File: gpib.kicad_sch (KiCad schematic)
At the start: 5 parts, among them U1 SN74LVC8T245PWR, U2 SN74LVC07APWR, U6 SN74LVC1G07DCKR, U7 SN74LVC14APWR

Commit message: Start work on PCB
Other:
- moved on the sheet: R8, U1, U2, U6, U7

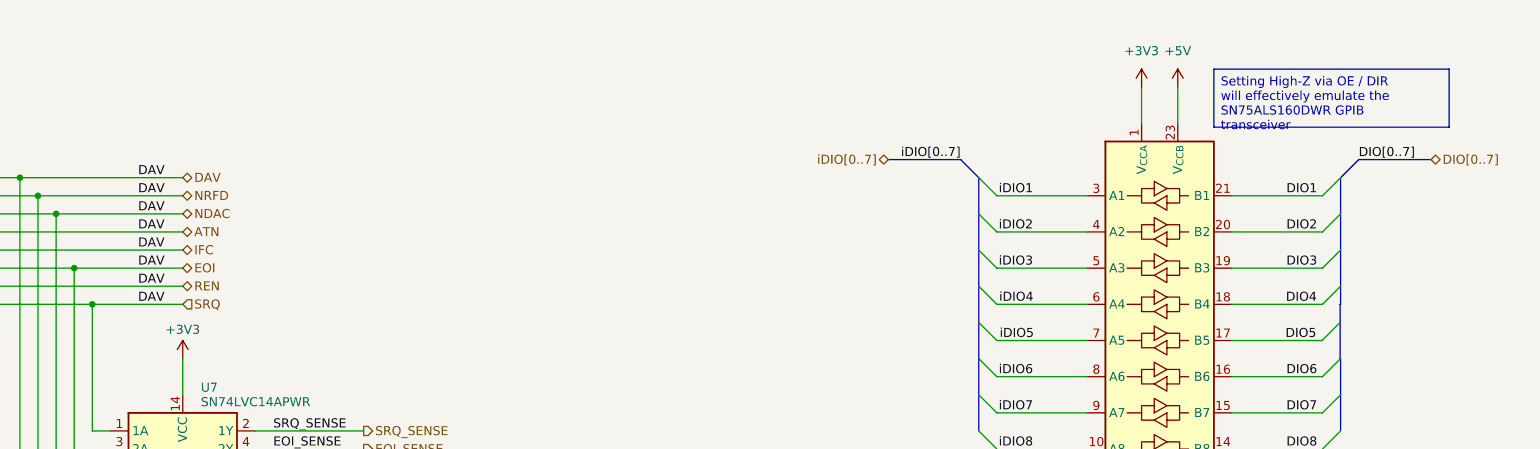
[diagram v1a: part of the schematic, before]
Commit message: Fix GPIB DIO bus nets and start PCB. Adjusted to 4 layers
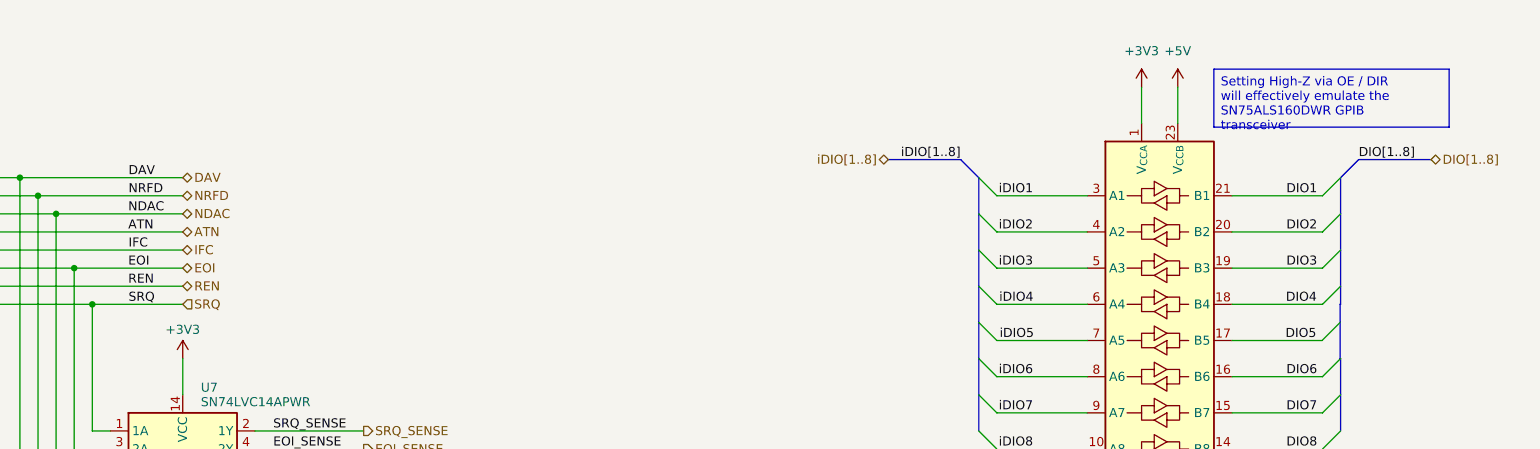
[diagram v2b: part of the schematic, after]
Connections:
- net ATN: no longer R8.1 (R1.1), R8.2 (R2.1), R8.3 (R3.1), R8.5 (R5.1), R8.6 (R6.1), R8.7 (R7.1), R8.8 (R8.1), U2.10 (5Y), U2.12 (6Y), U2.2 (1Y), U2.4 (2Y), U2.6 (3Y), U6.4 (Y), U7.1 (1A), U7.11 (5A), U7.3 (2A), U7.5 (3A), U7.9 (4A)
- new net DAV: R8.1 (R1.1), U2.2 (1Y), U7.11 (5A)
- new net EOI: R8.6 (R6.1), U2.12 (6Y), U7.3 (2A)
- new net IFC: R8.5 (R5.1), U2.10 (5Y)
- new net NDAC: R8.3 (R3.1), U2.6 (3Y), U7.5 (3A)
- new net NRFD: R8.2 (R2.1), U2.4 (2Y), U7.9 (4A)
- new net REN: R8.7 (R7.1), U6.4 (Y)
- new net SRQ: R8.8 (R8.1), U7.1 (1A)
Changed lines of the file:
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@@
+		)
+	)
+	(label "NDAC"
+		(at 170.1435 114.3 0)
+		(effects
+			(font
+				(size 1.27 1.27)
+			)
+			(justify left bottom)
 		)
 	)
@@
 		)
 	)
+	(label "EOI"
+		(at 170.1435 121.92 0)
+		(effects
+			(font
+				(size 1.27 1.27)
+			)
+			(justify left bottom)
+		)
+	)
 	(label "SRQ_SENSE"
 		(at 190.5 144.78 0)
@@
 		)
 	)
-	(label "DAV"
-		(at 175.2525 119.38 180)
-		(effects
-			(font
-				(size 1.27 1.27)
-			)
-			(justify right bottom)
+	(label "NRFD"
+		(at 170.18 111.76 0)
+		(effects
+			(font
+				(size 1.27 1.27)
+			)
+			(justify left bottom)
+		)
+	)
+	(label "SRQ"
+		(at 170.18 127 0)
+		(effects
+			(font
+				(size 1.27 1.27)
+			)
+			(justify left bottom)
 		)
 	)
@@
 		)
 	)
+	(label "ATN"
+		(at 170.1435 116.84 0)
+		(effects
+			(font
+				(size 1.27 1.27)
+			)
+			(justify left bottom)
+		)
+	)
 	(label "iDIO8"
 		(at 297.18 147.32 180)
@@
 		)
 	)
-	(label "DIO[0..7]"
+	(label "DIO[1..8]"
 		(at 342.9 106.68 0)
 		(effects
@@
 		)
 	)
-	(label "DAV"
-		(at 175.2525 127 180)
-		(effects
-			(font
-				(size 1.27 1.27)
-			)
-			(justify right bottom)
-		)
-	)
-	(label "DAV"
-		(at 175.2525 114.3 180)
-		(effects
-			(font
-				(size 1.27 1.27)
-			)
-			(justify right bottom)
-		)
-	)
 	(label "GPIB_EN"
 		(at 292.1 149.86 0)
@@
 		)
 	)
+	(label "IFC"
+		(at 170.18 119.38 0)
+		(effects
+			(font
+				(size 1.27 1.27)
+			)
+			(justify left bottom)
+		)
+	)
 	(label "GPIB_DIR"
 		(at 292.1 152.4 0)
@@
 		)
 	)
-	(label "DAV"
-		(at 175.2525 121.92 180)
-		(effects
-			(font
-				(size 1.27 1.27)
-			)
-			(justify right bottom)
-		)
-	)
 	(label "iDIO1"
 		(at 297.18 111.76 180)
@@
 		)
 	)
-	(label "DAV"
-		(at 175.2525 116.84 180)
-		(effects
-			(font
-				(size 1.27 1.27)
-			)
-			(justify right bottom)
-		)
-	)
-	(label "iDIO[0..7]"
+	(label "iDIO[1..8]"
 		(at 287.02 106.68 180)
 		(effects
@@
 		)
 	)
-	(label "DAV"
-		(at 175.26 124.46 180)
-		(effects
-			(font
-				(size 1.27 1.27)
-			)
-			(justify right bottom)
-		)
-	)
 	(label "iDIO4"
 		(at 297.2416 127 180)
@@
 	)
 	(label "DAV"
-		(at 175.26 109.22 180)
-		(effects
-			(font
-				(size 1.27 1.27)
-			)
-			(justify right bottom)
-		)
-	)
-	(label "DAV"
-		(at 175.26 111.76 180)
-		(effects
-			(font
-				(size 1.27 1.27)
-			)
-			(justify right bottom)
+		(at 170.18 109.22 0)
+		(effects
+			(font
+				(size 1.27 1.27)
+			)
+			(justify left bottom)
 		)
 	)
@@
 			)
 			(justify right bottom)
+		)
+	)
+	(label "REN"
+		(at 170.1435 124.46 0)
+		(effects
+			(font
+				(size 1.27 1.27)
+			)
+			(justify left bottom)
 		)
 	)
@@
 		)
 	)
-	(hierarchical_label "iDIO[0..7]"
+	(hierarchical_label "iDIO[1..8]"
 		(shape bidirectional)
 		(at 276.86 106.68 180)
@@
 		)
 	)
-	(hierarchical_label "DIO[0..7]"
+	(hierarchical_label "DIO[1..8]"
 		(shape bidirectional)
 		(at 353.06 106.68 0)

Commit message: Updates
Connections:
- net DIO1: now also U1.18 (B4); no longer U1.21 (B1)
- net DIO2: now also U1.19 (B3); no longer U1.20 (B2)
- net DIO3: now also U1.20 (B2); no longer U1.19 (B3)
- net DIO4: now also U1.21 (B1); no longer U1.18 (B4)
- net DIO5: now also U1.14 (B8); no longer U1.17 (B5)
- net DIO6: now also U1.15 (B7); no longer U1.16 (B6)
- net DIO7: now also U1.16 (B6); no longer U1.15 (B7)
- net DIO8: now also U1.17 (B5); no longer U1.14 (B8)
- net iDIO1: now also U1.6 (A4); no longer U1.3 (A1)
- net iDIO2: now also U1.5 (A3); no longer U1.4 (A2)
- net iDIO3: now also U1.4 (A2); no longer U1.5 (A3)
- net iDIO4: now also U1.3 (A1); no longer U1.6 (A4)
- net iDIO5: now also U1.10 (A8); no longer U1.7 (A5)
- net iDIO6: now also U1.9 (A7); no longer U1.8 (A6)
- net iDIO7: now also U1.8 (A6); no longer U1.9 (A7)
- net iDIO8: now also U1.7 (A5); no longer U1.10 (A8)
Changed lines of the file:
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@@
-		)
-	)
-	(label "DIO8"
-		(at 332.74 147.32 0)
-		(effects
-			(font
-				(size 1.27 1.27)
-			)
-			(justify left bottom)
 		)
 	)
@@
 		)
 	)
+	(label "DIO7"
+		(at 332.74 137.16 0)
+		(effects
+			(font
+				(size 1.27 1.27)
+			)
+			(justify left bottom)
+		)
+	)
 	(label "NDAC_SENSE"
 		(at 190.5 149.86 0)
@@
 		)
 	)
-	(label "DIO5"
-		(at 332.6168 132.08 0)
-		(effects
-			(font
-				(size 1.27 1.27)
-			)
-			(justify left bottom)
-		)
-	)
 	(label "iNDAC"
 		(at 92.71 114.3 180)
@@
 		)
 	)
-	(label "DIO7"
+	(label "DIO6"
 		(at 332.74 142.24 0)
 		(effects
@@
 		)
 	)
-	(label "DIO2"
-		(at 332.74 116.84 0)
-		(effects
-			(font
-				(size 1.27 1.27)
-			)
-			(justify left bottom)
-		)
-	)
-	(label "DIO4"
-		(at 332.6784 127 0)
-		(effects
-			(font
-				(size 1.27 1.27)
-			)
-			(justify left bottom)
-		)
-	)
 	(label "EOI"
 		(at 170.1435 121.92 0)
@@
 		)
 	)
+	(label "iDIO3"
+		(at 297.18 116.84 180)
+		(effects
+			(font
+				(size 1.27 1.27)
+			)
+			(justify right bottom)
+		)
+	)
 	(label "SRQ_SENSE"
 		(at 190.5 144.78 0)
@@
 		)
 	)
+	(label "iDIO7"
+		(at 297.18 137.16 180)
+		(effects
+			(font
+				(size 1.27 1.27)
+			)
+			(justify right bottom)
+		)
+	)
+	(label "DIO2"
+		(at 332.74 121.92 0)
+		(effects
+			(font
+				(size 1.27 1.27)
+			)
+			(justify left bottom)
+		)
+	)
 	(label "NRFD"
 		(at 170.18 111.76 0)
@@
 		)
 	)
-	(label "iDIO5"
-		(at 297.3032 132.08 180)
+	(label "iDIO2"
+		(at 297.18 121.92 180)
 		(effects
 			(font
@@
 		)
 	)
-	(label "iDIO8"
-		(at 297.18 147.32 180)
-		(effects
-			(font
-				(size 1.27 1.27)
-			)
-			(justify right bottom)
+	(label "iDIO6"
+		(at 297.18 142.24 180)
+		(effects
+			(font
+				(size 1.27 1.27)
+			)
+			(justify right bottom)
+		)
+	)
+	(label "DIO8"
+		(at 332.74 132.08 0)
+		(effects
+			(font
+				(size 1.27 1.27)
+			)
+			(justify left bottom)
 		)
 	)
@@
 		)
 	)
-	(label "iDIO7"
-		(at 297.18 142.24 180)
-		(effects
-			(font
-				(size 1.27 1.27)
-			)
-			(justify right bottom)
-		)
-	)
-	(label "DIO1"
+	(label "iDIO1"
+		(at 297.18 127 180)
+		(effects
+			(font
+				(size 1.27 1.27)
+			)
+			(justify right bottom)
+		)
+	)
+	(label "DIO4"
 		(at 332.74 111.76 0)
+		(effects
+			(font
+				(size 1.27 1.27)
+			)
+			(justify left bottom)
+		)
+	)
+	(label "DIO3"
+		(at 332.74 116.84 0)
 		(effects
 			(font
@@
 		)
 	)
-	(label "DIO3"
-		(at 332.74 121.92 0)
-		(effects
-			(font
-				(size 1.27 1.27)
-			)
-			(justify left bottom)
+	(label "iDIO8"
+		(at 297.0634 132.08 180)
+		(effects
+			(font
+				(size 1.27 1.27)
+			)
+			(justify right bottom)
 		)
 	)
@@
 		)
 	)
-	(label "iDIO6"
-		(at 297.18 137.16 180)
-		(effects
-			(font
-				(size 1.27 1.27)
-			)
-			(justify right bottom)
-		)
-	)
-	(label "iDIO1"
-		(at 297.18 111.76 180)
-		(effects
-			(font
-				(size 1.27 1.27)
-			)
-			(justify right bottom)
+	(label "DIO5"
+		(at 332.74 147.32 0)
+		(effects
+			(font
+				(size 1.27 1.27)
+			)
+			(justify left bottom)
 		)
 	)
@@
 		)
 	)
+	(label "DIO1"
+		(at 332.74 127 0)
+		(effects
+			(font
+				(size 1.27 1.27)
+			)
+			(justify left bottom)
+		)
+	)
+	(label "iDIO4"
+		(at 297.18 111.76 180)
+		(effects
+			(font
+				(size 1.27 1.27)
+			)
+			(justify right bottom)
+		)
+	)
 	(label "iDIO[1..8]"
 		(at 287.02 106.68 180)
@@
 		)
 	)
-	(label "iDIO3"
-		(at 297.18 121.92 180)
-		(effects
-			(font
-				(size 1.27 1.27)
-			)
-			(justify right bottom)
-		)
-	)
-	(label "DIO6"
-		(at 332.74 137.16 0)
-		(effects
-			(font
-				(size 1.27 1.27)
-			)
-			(justify left bottom)
-		)
-	)
-	(label "iDIO4"
-		(at 297.2416 127 180)
-		(effects
-			(font
-				(size 1.27 1.27)
-			)
-			(justify right bottom)
-		)
-	)
 	(label "DAV"
 		(at 170.18 109.22 0)
@@
 		)
 	)
-	(label "iDIO2"
-		(at 297.18 116.84 180)
-		(effects
-			(font
-				(size 1.27 1.27)
-			)
-			(justify right bottom)
-		)
-	)
 	(label "REN"
 		(at 170.1435 124.46 0)
@@
 		)
 	)
+	(label "iDIO5"
+		(at 297.18 147.32 180)
+		(effects
+			(font
+				(size 1.27 1.27)
+			)
+			(justify right bottom)
+		)
+	)

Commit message: Routing progress
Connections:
- net ATN: now also R8.1 (R1.1), U2.6 (3Y); no longer R8.4 (R4.1), U2.8 (4Y)
- net DAV: now also R8.6 (R6.1), U2.10 (5Y); no longer R8.1 (R1.1), U2.2 (1Y)
- net EOI: now also R8.7 (R7.1), U2.8 (4Y); no longer R8.6 (R6.1), U2.12 (6Y)
- net IFC: now also R8.3 (R3.1), U2.4 (2Y); no longer R8.5 (R5.1), U2.10 (5Y)
- net NDAC: now also R8.4 (R4.1), U2.2 (1Y); no longer R8.3 (R3.1), U2.6 (3Y)
- net NRFD: now also R8.5 (R5.1), U2.12 (6Y); no longer R8.2 (R2.1), U2.4 (2Y)
- net REN: now also R8.8 (R8.1); no longer R8.7 (R7.1)
- net SRQ: now also R8.2 (R2.1); no longer R8.8 (R8.1)
- net iATN: now also U2.5 (3A); no longer U2.9 (4A)
- net iDAV: now also U2.11 (5A); no longer U2.1 (1A)
- net iEOI: now also U2.9 (4A); no longer U2.13 (6A)
- net iIFC: now also U2.3 (2A); no longer U2.11 (5A)
- net iNDAC: now also U2.1 (1A); no longer U2.5 (3A)
- net iNRFD: now also U2.13 (6A); no longer U2.3 (2A)

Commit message: Final touches
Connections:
- net EOI: now also U7.5 (3A); no longer U7.3 (2A)
- net EOI_SENSE: now also U7.6 (3Y); no longer U7.4 (2Y)
- net NDAC: now also U7.3 (2A); no longer U7.5 (3A)
- net NDAC_SENSE: now also U7.4 (2Y); no longer U7.6 (3Y)
